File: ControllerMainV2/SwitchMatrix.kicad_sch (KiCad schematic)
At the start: 64 parts, among them IC1 MUX506IDWR, IC10 MUX506IDWR, IC11 MUX506IDWR, IC12 MUX506IDWR, IC13 MUX506IDWR, IC14 MUX506IDWR, IC15 MUX506IDWR, IC16 MUX506IDWR, IC2 MUX506IDWR, IC3 MUX506IDWR, IC4 MUX506IDWR, IC5 MUX506IDWR, IC6 MUX506IDWR, IC7 MUX506IDWR, IC8 MUX506IDWR, IC9 MUX506IDWR, U1 74HC595, U2 74HC595, U3 74HC595, U4 74HC595, U5 74HC595, U6 74HC595, U7 74HC595, U8 74HC595

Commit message: Added libs
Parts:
- removed C_U1, C_U2, C_U3, C_U4, C_U5, C_U6, C_U7, C_U8, C_VDD_IC1, C_VDD_IC10, C_VDD_IC11, C_VDD_IC12, C_VDD_IC13, C_VDD_IC14, C_VDD_IC15, C_VDD_IC16, C_VDD_IC2, C_VDD_IC3, C_VDD_IC4, C_VDD_IC5, C_VDD_IC6, C_VDD_IC7, C_VDD_IC8, C_VDD_IC9, C_VSS_IC1, C_VSS_IC10, C_VSS_IC11, C_VSS_IC12, C_VSS_IC13, C_VSS_IC14, C_VSS_IC15, C_VSS_IC16, C_VSS_IC2, C_VSS_IC3, C_VSS_IC4, C_VSS_IC5, C_VSS_IC6, C_VSS_IC7, C_VSS_IC8, C_VSS_IC9: 100n, Capacitor_SMD:C_1206_3216Metric_Pad1.33x1.80mm_HandSolder, symbol Device:C
- removed IC1, IC10, IC11, IC12, IC13, IC14, IC15, IC16, IC2, IC3, IC4, IC5, IC6, IC7, IC8, IC9: MUX506IDWR, SamacSys_Parts:SOIC127P1030X265-28N, symbol SamacSys_Parts:MUX506IDWR
- removed U1, U2, U3, U4, U5, U6, U7, U8: 74HC595, SamacSys_Parts:SOIC127P600X175-16N, symbol 74xx:74HC595
- added C19, C20, C26, C30: 100n, symbol Device:C
- added C28: (no value), symbol Device:C
- added D6: 1N4148, Diode_SMD:D_SOD-123, symbol Diode:1N4148
- added D7: (no value), symbol Diode:1N5818
- added D8: 1N5818, Diode_THT:D_DO-41_SOD81_P10.16mm_Horizontal, symbol Diode:1N5818
- added IC1: 1462039-4, SamacSys_Parts:14620394, symbol SamacSys_Parts:1462039-4
- added IC2: (no value), symbol SamacSys_Parts:TXU0104PWR
- added IC3: (no value), symbol SamacSys_Parts:AD75019JPZ
- added Q6: 2N7002, Package_TO_SOT_SMD:SOT-23, symbol Transistor_FET:2N7002
- added R62: 100k, Resistor_SMD:R_1206_3216Metric_Pad1.30x1.75mm_HandSolder, symbol Device:R
- added R63, R65, R66: 100k, symbol Device:R
- added R64: (no value), symbol Device:R
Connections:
- net GND: now also C19.2, C20.2, C26.2, C28.2, C30.2, D8.1 (K), IC1.2 (NC_1), IC2.5 (A4), IC2.7 (GND), IC3.43 (DGND), Q6.2 (S), R62.2, R64.2, R65.2, R66.2
- net In1: now also IC3.31 (Y0)
- net In10: now also IC3.13 (Y9)
- net In11: now also IC3.12 (Y10)
- net In12: now also IC3.11 (Y11)
- net In13: now also IC3.10 (Y12)
- net In14: now also IC3.9 (Y13)
- net In15: now also IC3.8 (Y14)
- net In16: now also IC3.7 (Y15)
- net In2: now also IC3.32 (Y1)
- net In3: now also IC3.33 (Y2)
- net In4: now also IC3.34 (Y3)
- net In5: now also IC3.35 (Y4)
- net In6: now also IC3.36 (Y5)
- net In7: now also IC3.37 (Y6)
- net In8: now also IC3.38 (Y7)
- net In9: now also IC3.14 (Y8)
- net Out1: now also IC3.15 (X0)
- net Out10: now also IC3.24 (X9)
- net Out11: now also IC3.25 (X10)
- net Out12: now also IC3.26 (X11)
- net Out13: now also IC3.27 (X12)
- net Out14: now also IC3.28 (X13)
- net Out15: now also IC3.29 (X14)
- net Out16: now also IC3.30 (X15)
- net Out2: now also IC3.16 (X1)
- net Out3: now also IC3.17 (X2)
- net Out4: now also IC3.18 (X3)
- net Out5: now also IC3.19 (X4)
- net Out6: now also IC3.20 (X5)
- net Out7: now also IC3.21 (X6)
- net Out8: now also IC3.22 (X7)
- net Out9: now also IC3.23 (X8)
- net VDD_15V0: now also C19.1, D7.1 (K), IC3.41 (VDD)
- net VDD_3V3: now also C26.1, C28.1, IC2.1 (VCCA)
- net VSS_15V0: now also C20.1, D8.2 (A), IC3.4 (VSS)
- new net: D6.2 (A), IC1.8 (-), Q6.3 (D)
- new net CS: IC2.8 (OE), R66.1
- new net EN_SPL_Matrix: Q6.1 (G), R62.1
- new net MOSI: IC2.3 (A2)
- new net MOSI_i: IC2.12 (B2Y), IC3.3 (SIN), R64.1
- new net RCLK: IC2.4 (A3)
- new net RCLK_i: IC2.11 (B3Y), IC3.1 (PCLK), R63.2
- new net SCLK: IC2.2 (A1)
- new net SCLK_i: IC2.13 (B1Y), IC3.2 (SCLK), R65.1
- new net VDD5V0_i: C30.1, D7.2 (A), IC1.3 (COM_1), IC2.14 (VCCB), IC3.42 (VCC), R63.1
- new net VDD_5V0: D6.1 (K), IC1.1 (+), IC1.4 (NO_1)
- no-connect marks 48 -> 11

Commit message: Main mostly wired. Push for replacement
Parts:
- removed C28: (no value), symbol Device:C
- C19, C20, C26, C30: footprint (none) -> Capacitor_SMD:C_1206_3216Metric_Pad1.33x1.80mm_HandSolder
- D7: value (none) -> 1N5818; footprint (none) -> Diode_SMD:D_SOD-123
- D8: footprint Diode_THT:D_DO-41_SOD81_P10.16mm_Horizontal -> Diode_SMD:D_SOD-123
- IC2: value (none) -> TXU0104PWR; footprint (none) -> SamacSys_Parts:SOP65P640X120-14N
- IC3: value (none) -> AD75019JPZ; footprint (none) -> Package_LCC:PLCC-44_SMD-Socket
- R63, R65, R66: footprint (none) -> Resistor_SMD:R_1206_3216Metric_Pad1.30x1.75mm_HandSolder
- R64: value (none) -> 100k; footprint (none) -> Resistor_SMD:R_1206_3216Metric_Pad1.30x1.75mm_HandSolder
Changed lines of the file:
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@@
   (junction (at 97.536 76.454) (diameter 0) (color 0 0 0 0)
-  )
-  (junction (at 50.292 61.214) (diameter 0) (color 0 0 0 0)
   )
   (junction (at 259.08 45.72) (diameter 0) (color 0 0 0 0)
@@
     (stroke (width 0) (type default) (color 0 0 0 0))
   )
-  (wire (pts (xy 50.292 63.754) (xy 50.292 61.214))
-    (stroke (width 0) (type default) (color 0 0 0 0))
-  )
   (wire (pts (xy 227.584 89.154) (xy 227.584 91.694))
     (stroke (width 0) (type default) (color 0 0 0 0))
@@
     (stroke (width 0) (type default) (color 0 0 0 0))
   )
-  (wire (pts (xy 50.292 61.214) (xy 68.072 61.214))
+  (wire (pts (xy 45.466 61.214) (xy 68.072 61.214))
     (stroke (width 0) (type default) (color 0 0 0 0))
   )
@@
     (stroke (width 0) (type default) (color 0 0 0 0))
   )
-  (wire (pts (xy 50.292 72.644) (xy 50.292 71.374))
-    (stroke (width 0) (type default) (color 0 0 0 0))
-  )
   (wire (pts (xy 151.13 163.83) (xy 151.13 166.37))
     (stroke (width 0) (type default) (color 0 0 0 0))
@@
   )
   (wire (pts (xy 138.43 125.73) (xy 140.97 125.73))
-    (stroke (width 0) (type default) (color 0 0 0 0))
-  )
-  (wire (pts (xy 45.466 61.214) (xy 50.292 61.214))
     (stroke (width 0) (type default) (color 0 0 0 0))
   )
@@
       (effects (font (size 1.27 1.27)) (justify right))
     )
-    (property "Value" "" (id 1) (at 207.01 99.0477 90)
+    (property "Value" "1N5818" (id 1) (at 207.01 99.0477 90)
       (effects (font (size 1.27 1.27)) (justify right))
     )
-    (property "Footprint" "" (id 2) (at 209.423 97.028 0)
+    (property "Footprint" "Diode_SMD:D_SOD-123" (id 2) (at 209.423 97.028 0)
       (effects (font (size 1.27 1.27)) hide)
     )
@@
     (in_bom yes) (on_board yes) (fields_autoplaced)
     (property "Reference" "IC2" (id 0) (at 82.042 55.025 0))
-    (property "Value" "" (id 1) (at 82.042 57.5619 0))
-    (property "Footprint" "" (id 2) (at 92.202 58.674 0)
+    (property "Value" "TXU0104PWR" (id 1) (at 82.042 57.5619 0))
+    (property "Footprint" "SamacSys_Parts:SOP65P640X120-14N" (id 2) (at 92.202 58.674 0)
       (effects (font (size 1.27 1.27)) (justify left) hide)
     )
@@
       (effects (font (size 1.27 1.27)) (justify left))
     )
-    (property "Footprint" "" (id 2) (at 186.8932 97.282 0)
+    (property "Footprint" "Capacitor_SMD:C_1206_3216Metric_Pad1.33x1.80mm_HandSolder" (id 2) (at 186.8932 97.282 0)
       (effects (font (size 1.27 1.27)) hide)
     )
@@
       (effects (font (size 1.27 1.27)) (justify left))
     )
-    (property "Footprint" "" (id 2) (at 123.19 76.962 90)
+    (property "Footprint" "Resistor_SMD:R_1206_3216Metric_Pad1.30x1.75mm_HandSolder" (id 2) (at 123.19 76.962 90)
       (effects (font (size 1.27 1.27)) hide)
     )
@@
       (effects (font (size 1.27 1.27)) (justify left))
     )
-    (property "Footprint" "" (id 2) (at 71.0692 36.322 0)
+    (property "Footprint" "Capacitor_SMD:C_1206_3216Metric_Pad1.33x1.80mm_HandSolder" (id 2) (at 71.0692 36.322 0)
       (effects (font (size 1.27 1.27)) hide)
     )
@@
     (pin "8")
   )
-  (symbol (lib_id "power:GND") (at 50.292 72.644 0) (unit 1)
-    (in_bom yes) (on_board yes) (fields_autoplaced)
-    (property "Reference" "#PWR048" (id 0) (at 50.292 78.994 0)
-      (effects (font (size 1.27 1.27)) hide)
-    )
-    (property "Value" "GND" (id 1) (at 50.292 77.0874 0))
-    (property "Footprint" "" (id 2) (at 50.292 72.644 0)
-      (effects (font (size 1.27 1.27)) hide)
-    )
-    (property "Datasheet" "" (id 3) (at 50.292 72.644 0)
-      (effects (font (size 1.27 1.27)) hide)
-    )
-    (pin "1")
-  )
   (symbol (lib_id "power:GND") (at 124.968 82.042 0) (unit 1)
     (in_bom yes) (on_board yes) (fields_autoplaced)
@@
     (in_bom yes) (on_board yes) (fields_autoplaced)
     (property "Reference" "IC3" (id 0) (at 183.2472 117.4835 0))
-    (property "Value" "" (id 1) (at 183.2472 120.0204 0))
-    (property "Footprint" "" (id 2) (at 177.8 113.03 0)
+    (property "Value" "AD75019JPZ" (id 1) (at 183.2472 120.0204 0))
+    (property "Footprint" "Package_LCC:PLCC-44_SMD-Socket" (id 2) (at 177.8 113.03 0)
       (effects (font (size 1.27 1.27)) (justify left) hide)
     )
@@
     (pin "9")
   )
-  (symbol (lib_id "Device:C") (at 50.292 67.564 0) (unit 1)
-    (in_bom yes) (on_board yes) (fields_autoplaced)
-    (property "Reference" "C28" (id 0) (at 53.213 66.7293 0)
-      (effects (font (size 1.27 1.27)) (justify left))
-    )
-    (property "Value" "" (id 1) (at 53.213 69.2662 0)
-      (effects (font (size 1.27 1.27)) (justify left))
-    )
-    (property "Footprint" "" (id 2) (at 51.2572 71.374 0)
-      (effects (font (size 1.27 1.27)) hide)
-    )
-    (property "Datasheet" "~" (id 3) (at 50.292 67.564 0)
-      (effects (font (size 1.27 1.27)) hide)
-    )
-    (pin "1")
-    (pin "2")
-  )
   (symbol (lib_id "power:GND") (at 80.01 37.592 0) (unit 1)
     (in_bom yes) (on_board yes) (fields_autoplaced)
@@
       (effects (font (size 1.27 1.27)) (justify left))
     )
-    (property "Footprint" "" (id 2) (at 95.758 87.122 90)
+    (property "Footprint" "Resistor_SMD:R_1206_3216Metric_Pad1.30x1.75mm_HandSolder" (id 2) (at 95.758 87.122 90)
       (effects (font (size 1.27 1.27)) hide)
     )
@@
       (effects (font (size 1.27 1.27)) (justify left))
     )
-    (property "Footprint" "" (id 2) (at 80.9752 36.322 0)
+    (property "Footprint" "Capacitor_SMD:C_1206_3216Metric_Pad1.33x1.80mm_HandSolder" (id 2) (at 80.9752 36.322 0)
       (effects (font (size 1.27 1.27)) hide)
     )
@@
       (effects (font (size 1.27 1.27)) (justify left))
     )
-    (property "Footprint" "" (id 2) (at 119.634 54.61 90)
+    (property "Footprint" "Resistor_SMD:R_1206_3216Metric_Pad1.30x1.75mm_HandSolder" (id 2) (at 119.634 54.61 90)
       (effects (font (size 1.27 1.27)) hide)
     )
@@
       (effects (font (size 1.27 1.27)) (justify left))
     )
-    (property "Value" "" (id 1) (at 118.618 78.6642 0)
-      (effects (font (size 1.27 1.27)) (justify left))
-    )
-    (property "Footprint" "" (id 2) (at 115.062 76.962 90)
+    (property "Value" "100k" (id 1) (at 118.618 78.6642 0)
+      (effects (font (size 1.27 1.27)) (justify left))
+    )
+    (property "Footprint" "Resistor_SMD:R_1206_3216Metric_Pad1.30x1.75mm_HandSolder" (id 2) (at 115.062 76.962 90)
       (effects (font (size 1.27 1.27)) hide)
     )
@@
       (effects (font (size 1.27 1.27)) (justify left))
     )
-    (property "Footprint" "" (id 2) (at 61.1632 36.322 0)
+    (property "Footprint" "Capacitor_SMD:C_1206_3216Metric_Pad1.33x1.80mm_HandSolder" (id 2) (at 61.1632 36.322 0)
       (effects (font (size 1.27 1.27)) hide)
     )
@@
       (effects (font (size 1.27 1.27)) (justify left))
     )
-    (property "Footprint" "Diode_THT:D_DO-41_SOD81_P10.16mm_Horizontal" (id 2) (at 212.725 97.028 0)
-      (effects (font (size 1.27 1.27)) hide)
-    )
+    (property "Footprint" "Diode_SMD:D_SOD-123" (id 2) (at 212.725 97.028 0)
+      (effects (font (size 1.27 1.27)) hide)
+    )

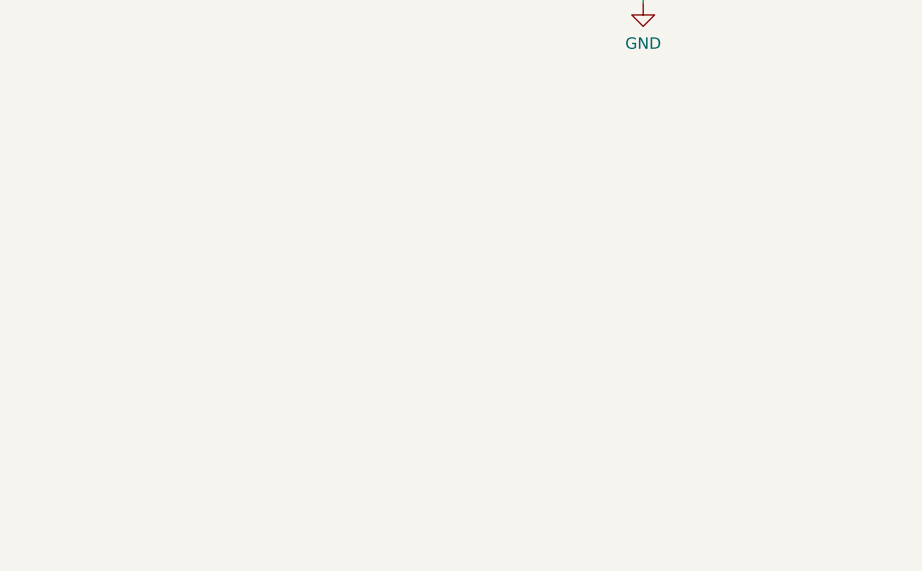
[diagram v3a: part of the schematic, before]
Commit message: Added pin header for matrix test
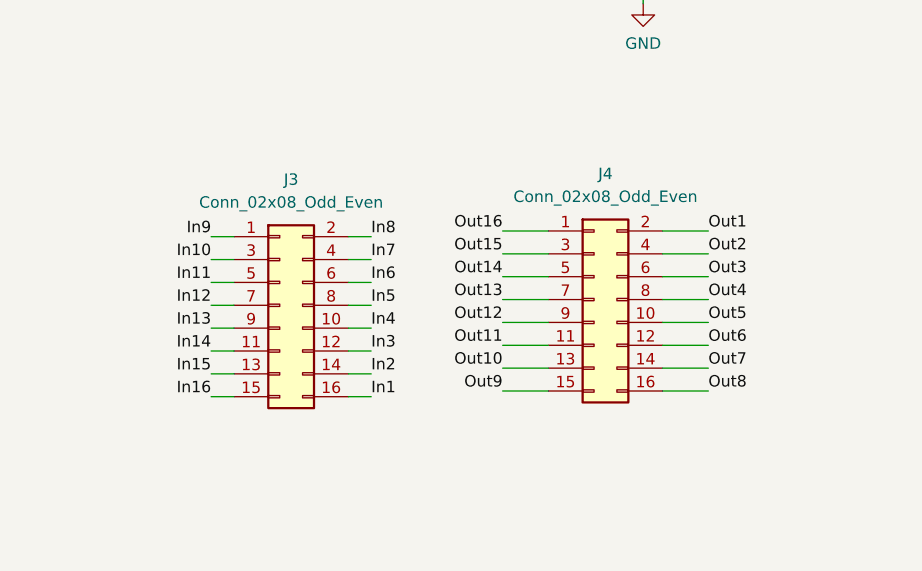
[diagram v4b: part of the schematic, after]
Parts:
- added J3, J4: Conn_02x08_Odd_Even, Connector_PinHeader_1.27mm:PinHeader_2x08_P1.27mm_Vertical_SMD, symbol Connector_Generic:Conn_02x08_Odd_Even
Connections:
- net In1: now also J3.16 (Pin_16)
- net In10: now also J3.3 (Pin_3)
- net In11: now also J3.5 (Pin_5)
- net In12: now also J3.7 (Pin_7)
- net In13: now also J3.9 (Pin_9)
- net In14: now also J3.11 (Pin_11)
- net In15: now also J3.13 (Pin_13)
- net In16: now also J3.15 (Pin_15)
- net In2: now also J3.14 (Pin_14)
- net In3: now also J3.12 (Pin_12)
- net In4: now also J3.10 (Pin_10)
- net In5: now also J3.8 (Pin_8)
- net In6: now also J3.6 (Pin_6)
- net In7: now also J3.4 (Pin_4)
- net In8: now also J3.2 (Pin_2)
- net In9: now also J3.1 (Pin_1)
- net Out1: now also J4.2 (Pin_2)
- net Out10: now also J4.13 (Pin_13)
- net Out11: now also J4.11 (Pin_11)
- net Out12: now also J4.9 (Pin_9)
- net Out13: now also J4.7 (Pin_7)
- net Out14: now also J4.5 (Pin_5)
- net Out15: now also J4.3 (Pin_3)
- net Out16: now also J4.1 (Pin_1)
- net Out2: now also J4.4 (Pin_4)
- net Out3: now also J4.6 (Pin_6)
- net Out4: now also J4.8 (Pin_8)
- net Out5: now also J4.10 (Pin_10)
- net Out6: now also J4.12 (Pin_12)
- net Out7: now also J4.14 (Pin_14)
- net Out8: now also J4.16 (Pin_16)
- net Out9: now also J4.15 (Pin_15)

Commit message: 3D models and fixed pcbs
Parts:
- IC3: footprint Package_LCC:PLCC-44_SMD-Socket -> SamacSys_Parts:69802144LF
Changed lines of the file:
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@@
     (property "Reference" "IC3" (id 0) (at 183.2472 117.4835 0))
     (property "Value" "AD75019JPZ" (id 1) (at 183.2472 120.0204 0))
-    (property "Footprint" "Package_LCC:PLCC-44_SMD-Socket" (id 2) (at 177.8 113.03 0)
+    (property "Footprint" "SamacSys_Parts:69802144LF" (id 2) (at 177.8 113.03 0)
       (effects (font (size 1.27 1.27)) (justify left) hide)
     )
